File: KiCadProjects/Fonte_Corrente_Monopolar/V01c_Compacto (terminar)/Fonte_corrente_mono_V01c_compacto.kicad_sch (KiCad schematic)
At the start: 20 parts, among them J1 Entrada, J2 Saída, J3 Nós, U1 AD828AN, U2 INA128

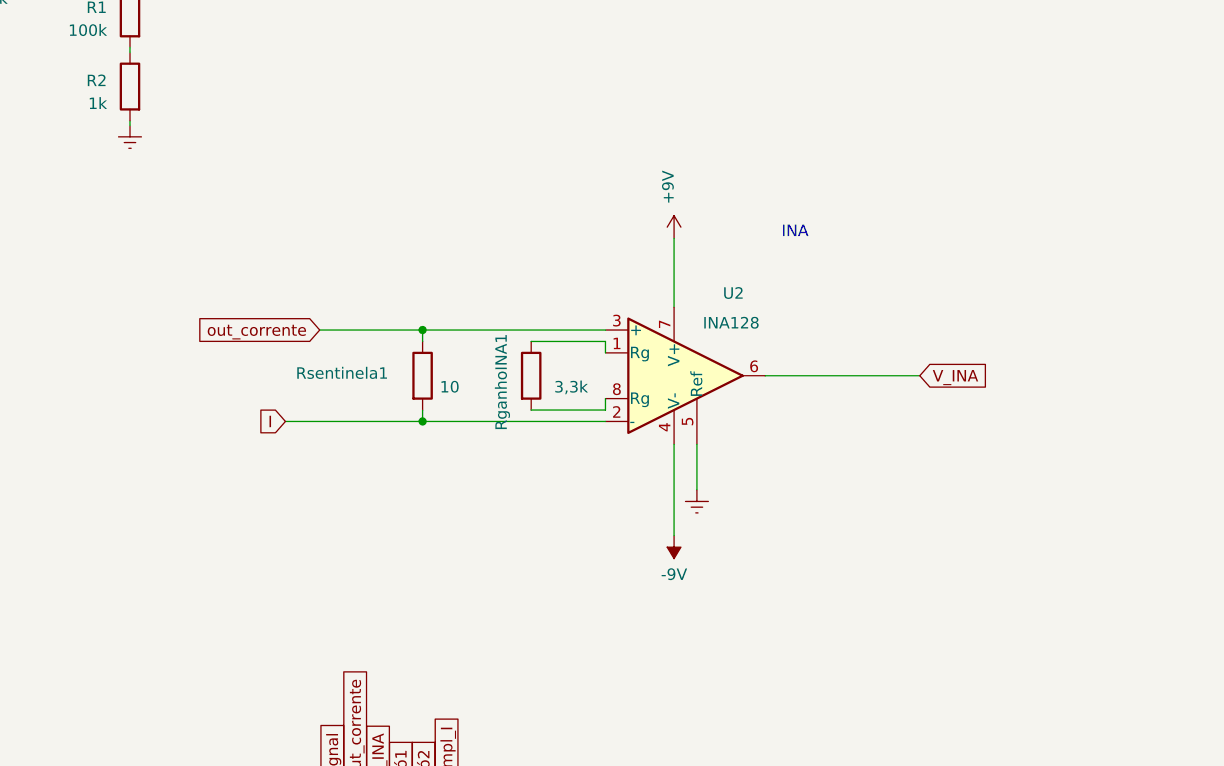
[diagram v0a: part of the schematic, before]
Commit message: correcao vcc vee ina
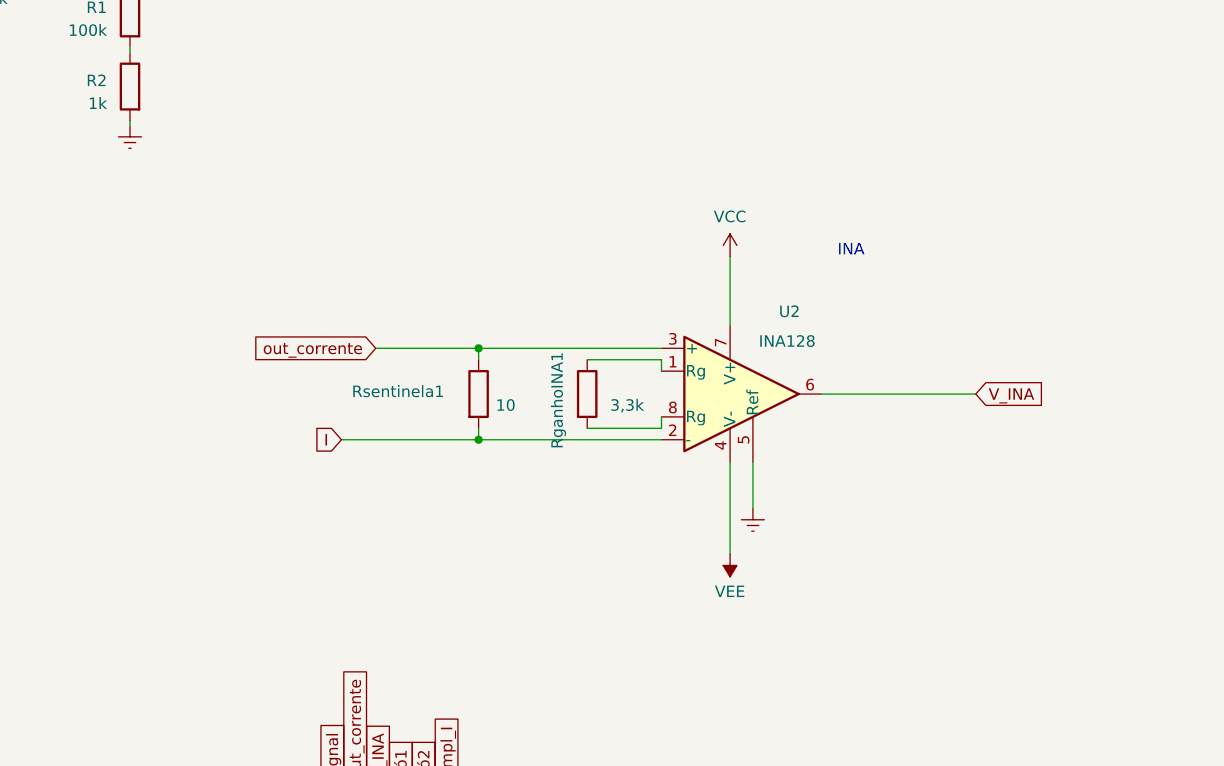
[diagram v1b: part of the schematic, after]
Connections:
- net +9V is gone; now on net VCC: U2.7 (V+)
- net -9V is gone; now on net VEE: U2.4 (V-)
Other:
- moved on the sheet: RganhoINA1, Rsentinela1, U2
